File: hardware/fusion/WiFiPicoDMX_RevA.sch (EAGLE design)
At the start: 38 parts, among them J1 JST XH B4B-XH-A DMX: COM,-,+,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, J2 JST XH B5B-XH-A MIDI: 1,2,3,4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, J3 FREE GPIO PADS, J4 ANALOG PADS, J5 RESERVED SIGNAL TEST PADS, J6 POWER/DMX TEST PADS, SW1 PTS810SJM250SMTR LFS RESET (N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, U1 Raspberry Pi Pico 2 W, U2 ISOW1412DFMR, U3 HCPL-0700-500E

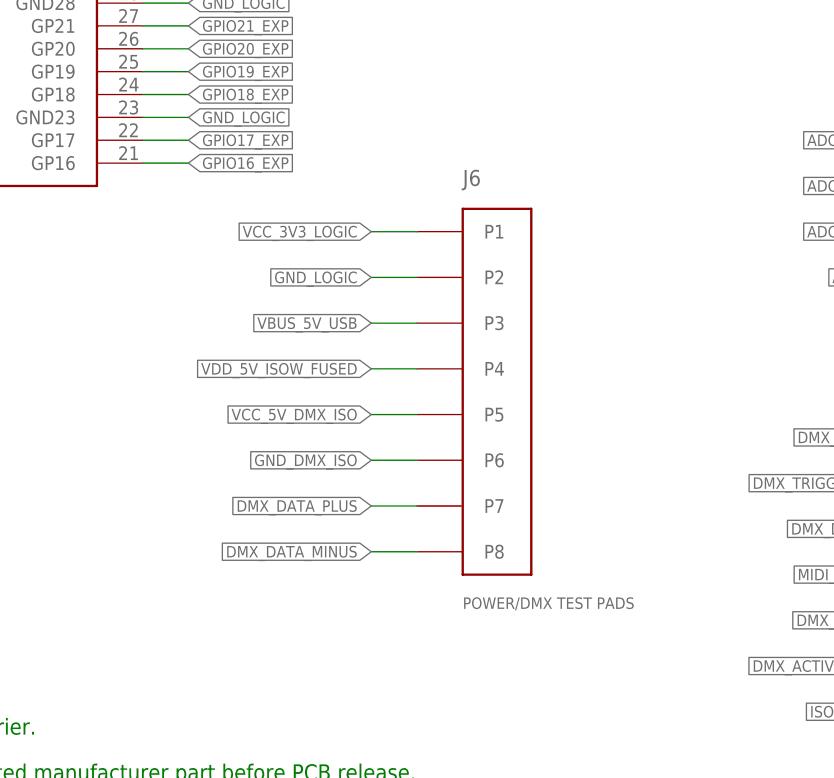
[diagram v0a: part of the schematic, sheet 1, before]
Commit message: hardware: synchronize manual board placement
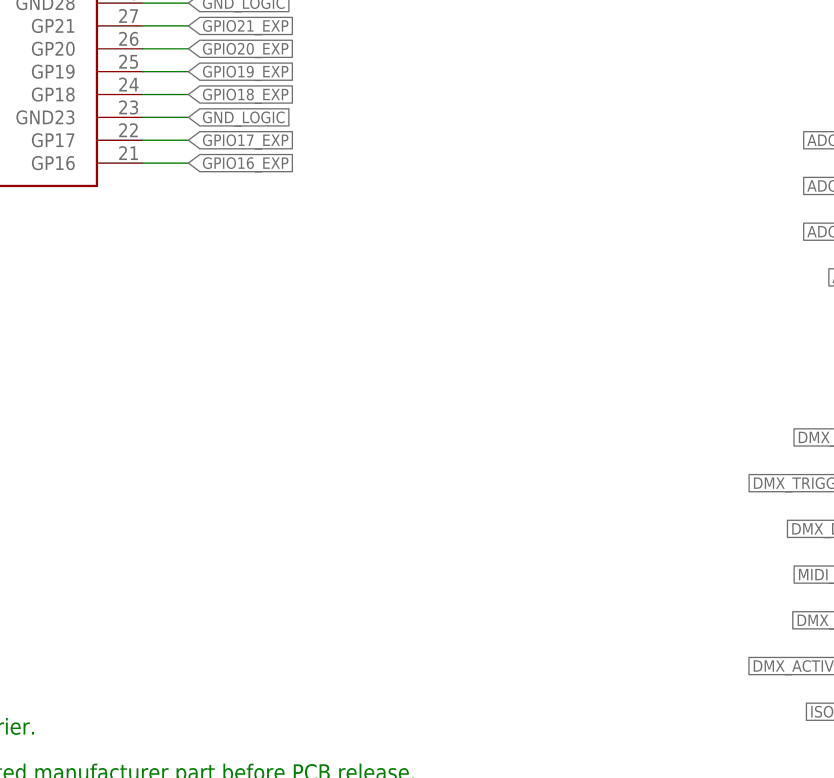
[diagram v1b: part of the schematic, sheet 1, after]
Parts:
- removed J6: POWER/DMX TEST PADS, WiFiPicoDMX_RevA_embedded:PADBANK8
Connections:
- net DMX_DATA_MINUS: no longer J6.P8
- net DMX_DATA_PLUS: no longer J6.P7
- net GND_DMX_ISO: no longer J6.P6
- net GND_LOGIC: no longer J6.P2
- net VBUS_5V_USB: no longer J6.P3
- net VCC_3V3_LOGIC: no longer J6.P1
- net VCC_5V_DMX_ISO: no longer J6.P5
- net VDD_5V_ISOW_FUSED: no longer J6.P4
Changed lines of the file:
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@@
         <part name="J4" library="WiFiPicoDMX_RevA_embedded" deviceset="PADBANK5" device="" value="ANALOG PADS"/>
         <part name="J5" library="WiFiPicoDMX_RevA_embedded" deviceset="PADBANK7" device="" value="RESERVED SIGNAL TEST PADS"/>
-        <part name="J6" library="WiFiPicoDMX_RevA_embedded" deviceset="PADBANK8" device="" value="POWER/DMX TEST PADS"/>
         <part name="U2" library="WiFiPicoDMX_RevA_embedded" deviceset="ISOW1412DFMR" device="" value="ISOW1412DFMR"/>
         <part name="R1" library="WiFiPicoDMX_RevA_embedded" deviceset="RES0402" device="" value="100k 1% 0.063W 0402 Yageo RC0402FR-07100KL"/>
@@
                     <instance part="J4" gate="G$1" x="213.36" y="71.12" rot="R0" smashed="no"/>
                     <instance part="J5" gate="G$1" x="213.36" y="33.02" rot="R0" smashed="no"/>
-                    <instance part="J6" gate="G$1" x="152.4" y="53.34" rot="R0" smashed="no"/>
                   </instances>
                   <busses/>
@@
                                                   </segment>
                                 </net>
-                    <net name="DMX_DATA_MINUS" class="0">
-                                  <segment>
-                                                    <pinref part="J6" gate="G$1" pin="P8"/>
-                                                    <wire x1="147.32" y1="35.56" x2="142.23999999999998" y2="35.56" width="0.1524" layer="91"/>
-                                                    <label x="142.23999999999998" y="35.56" size="1.27" layer="95" xref="yes" rot="R180"/>
-                                                  </segment>
-                                </net>
-                    <net name="DMX_DATA_PLUS" class="0">
-                                  <segment>
-                                                    <pinref part="J6" gate="G$1" pin="P7"/>
-                                                    <wire x1="147.32" y1="40.64" x2="142.23999999999998" y2="40.64" width="0.1524" layer="91"/>
-                                                    <label x="142.23999999999998" y="40.64" size="1.27" layer="95" xref="yes" rot="R180"/>
-                                                  </segment>
-                                </net>
                     <net name="DMX_DIR_GPIO4" class="0">
                                   <segment>
@@
                                                   </segment>
                                 </net>
-                    <net name="GND_DMX_ISO" class="0">
-                                  <segment>
-                                                    <pinref part="J6" gate="G$1" pin="P6"/>
-                                                    <wire x1="147.32" y1="45.720000000000006" x2="142.23999999999998" y2="45.720000000000006" width="0.1524" layer="91"/>
-                                                    <label x="142.23999999999998" y="45.720000000000006" size="1.27" layer="95" xref="yes" rot="R180"/>
-                                                  </segment>
-                                </net>
                     <net name="GND_LOGIC" class="0">
                                   <segment>
@@
                                                     <label x="261.62" y="124.46" size="1.27" layer="95" xref="yes"/>
                                                   </segment>
-                                  <segment>
-                                                    <pinref part="J6" gate="G$1" pin="P2"/>
-                                                    <wire x1="147.32" y1="66.04" x2="142.23999999999998" y2="66.04" width="0.1524" layer="91"/>
-                                                    <label x="142.23999999999998" y="66.04" size="1.27" layer="95" xref="yes" rot="R180"/>
-                                                  </segment>
                                 </net>
                     <net name="GPIO0_EXP" class="0">
@@
                                                     <label x="126.99999999999999" y="172.72" size="1.27" layer="95" xref="yes" rot="R180"/>
                                                   </segment>
-                                  <segment>
-                                                    <pinref part="J6" gate="G$1" pin="P3"/>
-                                                    <wire x1="147.32" y1="60.96" x2="142.23999999999998" y2="60.96" width="0.1524" layer="91"/>
-                                                    <label x="142.23999999999998" y="60.96" size="1.27" layer="95" xref="yes" rot="R180"/>
-                                                  </segment>
                                 </net>
                     <net name="VCC_3V3_LOGIC" class="0">
@@
                                                   </segment>
                                   <segment>
-                                                    <pinref part="J6" gate="G$1" pin="P1"/>
-                                                    <wire x1="147.32" y1="71.12" x2="142.23999999999998" y2="71.12" width="0.1524" layer="91"/>
-                                                    <label x="142.23999999999998" y="71.12" size="1.27" layer="95" xref="yes" rot="R180"/>
-                                                  </segment>
-                                  <segment>
                                                     <pinref part="R8" gate="G$1" pin="1"/>
                                                     <wire x1="127.00000000000001" y1="139.7" x2="121.92000000000002" y2="139.7" width="0.1524" layer="91"/>
@@
                                                   </segment>
                                 </net>
-                    <net name="VCC_5V_DMX_ISO" class="0">
-                                  <segment>
-                                                    <pinref part="J6" gate="G$1" pin="P5"/>
-                                                    <wire x1="147.32" y1="50.800000000000004" x2="142.23999999999998" y2="50.800000000000004" width="0.1524" layer="91"/>
-                                                    <label x="142.23999999999998" y="50.800000000000004" size="1.27" layer="95" xref="yes" rot="R180"/>
-                                                  </segment>
-                                </net>
                     <net name="VDD_5V_ISOW_FUSED" class="0">
                                   <segment>
@@
                                                     <label x="147.32000000000002" y="172.72" size="1.27" layer="95" xref="yes"/>
                                                   </segment>
-                                  <segment>
-                                                    <pinref part="J6" gate="G$1" pin="P4"/>
-                                                    <wire x1="147.32" y1="55.88" x2="142.23999999999998" y2="55.88" width="0.1524" layer="91"/>
-                                                    <label x="142.23999999999998" y="55.88" size="1.27" layer="95" xref="yes" rot="R180"/>
-                                                  </segment>
-                                </net>
+                                </net>

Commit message: hardware: link Fusion design to used component library
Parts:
- C1, C2, C4, C6, C7: device WiFiPicoDMX_RevA_embedded:CAP0402 -> WiFiPicoDMX_RevA_used:CAP0402
- C3, C5: device WiFiPicoDMX_RevA_embedded:CAP0805 -> WiFiPicoDMX_RevA_used:CAP0805
- C8, C9: device WiFiPicoDMX_RevA_embedded:CAP0603 -> WiFiPicoDMX_RevA_used:CAP0603
- D1: device WiFiPicoDMX_RevA_embedded:SM712 -> WiFiPicoDMX_RevA_used:SM712
- D2: device WiFiPicoDMX_RevA_embedded:DIODE_SOD323 -> WiFiPicoDMX_RevA_used:DIODE_SOD323
- D3, D4: device WiFiPicoDMX_RevA_embedded:LED0603 -> WiFiPicoDMX_RevA_used:LED0603
- F1: device WiFiPicoDMX_RevA_embedded:PPTC1206 -> WiFiPicoDMX_RevA_used:PPTC1206
- FB1, FB2: device WiFiPicoDMX_RevA_embedded:FERRITE0402 -> WiFiPicoDMX_RevA_used:FERRITE0402
- J1: device WiFiPicoDMX_RevA_embedded:PANEL_DMX4 -> WiFiPicoDMX_RevA_used:PANEL_DMX4
- J2: device WiFiPicoDMX_RevA_embedded:PANEL_MIDI5 -> WiFiPicoDMX_RevA_used:PANEL_MIDI5
- J3: device WiFiPicoDMX_RevA_embedded:PADBANK17 -> WiFiPicoDMX_RevA_used:PADBANK17
- J4: device WiFiPicoDMX_RevA_embedded:PADBANK5 -> WiFiPicoDMX_RevA_used:PADBANK5
- J5: device WiFiPicoDMX_RevA_embedded:PADBANK7 -> WiFiPicoDMX_RevA_used:PADBANK7
- L1: device WiFiPicoDMX_RevA_embedded:CMC_OPTION -> WiFiPicoDMX_RevA_used:CMC_OPTION
- R1, R10, R11, R2, R3, R4, R5, R6, R7, R8, R9: device WiFiPicoDMX_RevA_embedded:RES0402 -> WiFiPicoDMX_RevA_used:RES0402
- SW1: device WiFiPicoDMX_RevA_embedded:SWITCH_SMD -> WiFiPicoDMX_RevA_used:SWITCH_SMD
- U1: device WiFiPicoDMX_RevA_embedded:PICO2W -> WiFiPicoDMX_RevA_used:PICO2W
- U2: device WiFiPicoDMX_RevA_embedded:ISOW1412DFMR -> WiFiPicoDMX_RevA_used:ISOW1412DFMR
- U3: device WiFiPicoDMX_RevA_embedded:HCPL_0700_500E -> WiFiPicoDMX_RevA_used:HCPL_0700_500E
